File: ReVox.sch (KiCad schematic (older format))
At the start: 43 parts, among them CN1 EXPANSION_PORT, CN2 AUDIO_OUT, CN3 AUDIO_OUT, U1 GAL20V8, U2 74LS273, U3 LM386

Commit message: RIP
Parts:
- removed C6: 100n, Capacitor_THT:C_Disc_D7.0mm_W2.5mm_P5.00mm, symbol Device:C
- added J1: CONN_SIGNALS, ReVox:PinHeader_2x25_P1.27mm_Vertical, symbol Connector_Generic:Conn_02x25_Odd_Even
- CN2, CN3: footprint ReSeed:AudioJack_SJ1-3525N -> ReVox:AudioJack_SJ1-3525N
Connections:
- net +5V: now also J1.3 (Pin_3), J1.5 (Pin_5)
- net GND: now also J1.1 (Pin_1), J1.2 (Pin_2), J1.49 (Pin_49), J1.50 (Pin_50)
- net a0: now also J1.42 (Pin_42)
- net a1: now also J1.40 (Pin_40)
- net a10: now also J1.22 (Pin_22)
- net a11: now also J1.20 (Pin_20)
- net a12: now also J1.18 (Pin_18)
- net a13: now also J1.16 (Pin_16)
- net a14: now also J1.14 (Pin_14)
- net a15: now also J1.12 (Pin_12)
- net a2: now also J1.38 (Pin_38)
- net a3: now also J1.36 (Pin_36)
- net a4: now also J1.34 (Pin_34)
- net a5: now also J1.32 (Pin_32)
- net a6: now also J1.30 (Pin_30)
- net a7: now also J1.28 (Pin_28)
- net a8: now also J1.26 (Pin_26)
- net a9: now also J1.24 (Pin_24)
- net d0: now also J1.41 (Pin_41)
- net d1: now also J1.39 (Pin_39)
- net d2: now also J1.37 (Pin_37)
- net d3: now also J1.35 (Pin_35)
- net d4: now also J1.33 (Pin_33)
- net d5: now also J1.31 (Pin_31)
- net d6: now also J1.29 (Pin_29)
- net d7: now also J1.27 (Pin_27)
- net ext_audio: now also J1.45 (Pin_45)
- net phi2: now also J1.47 (Pin_47)
- net r_~w: now also J1.9 (Pin_9)
- net ~reset: now also J1.6 (Pin_6)
- net ~cs0: now reaches CN1.10 (/CS0)
- net ~cs0: now also J1.19 (Pin_19)
- net ~cas: now reaches CN1.11 (/CAS)
- net ~cas: now also J1.21 (Pin_21)
- net mux: now reaches CN1.12 (MUX)
- net mux: now also J1.23 (Pin_23)
- net ba: now reaches CN1.13 (BA)
- net ba: now also J1.25 (Pin_25)
- net aec: now reaches CN1.22 (AEC)
- net aec: now also J1.43 (Pin_43)
- net ~irq: now reaches CN1.4 (/IRQ)
- net ~irq: now also J1.7 (Pin_7)
- net c1hi: now reaches CN1.6 (C1HI)
- net c1hi: now also J1.11 (Pin_11)
- net c2lo: now reaches CN1.7 (C2LOW)
- net c2lo: now also J1.13 (Pin_13)
- net c2hi: now reaches CN1.8 (C2HI)
- net c2hi: now also J1.15 (Pin_15)
- net ~cs1: now reaches CN1.9 (/CS1)
- net ~cs1: now also J1.17 (Pin_17)
- net aa: now reaches CN1.AA (NC)
- net aa: now also J1.46 (Pin_46)
- net c1lo: now reaches CN1.B (C1LOW)
- net c1lo: now also J1.4 (Pin_4)
- net bb: now reaches CN1.BB (NC)
- net bb: now also J1.48 (Pin_48)
- net ~ras: now reaches CN1.D (/RAS)
- net ~ras: now also J1.8 (Pin_8)
- net phi0: now reaches CN1.E (PHI0)
- net phi0: now also J1.10 (Pin_10)
- net z: now reaches CN1.Z (NC)
- net z: now also J1.44 (Pin_44)
- no-connect marks 17 -> 4
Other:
- note added: "HELPS WITH SCOPING\nAND ROUTING"
- moved on the sheet: CN1, JP1, U1, U2

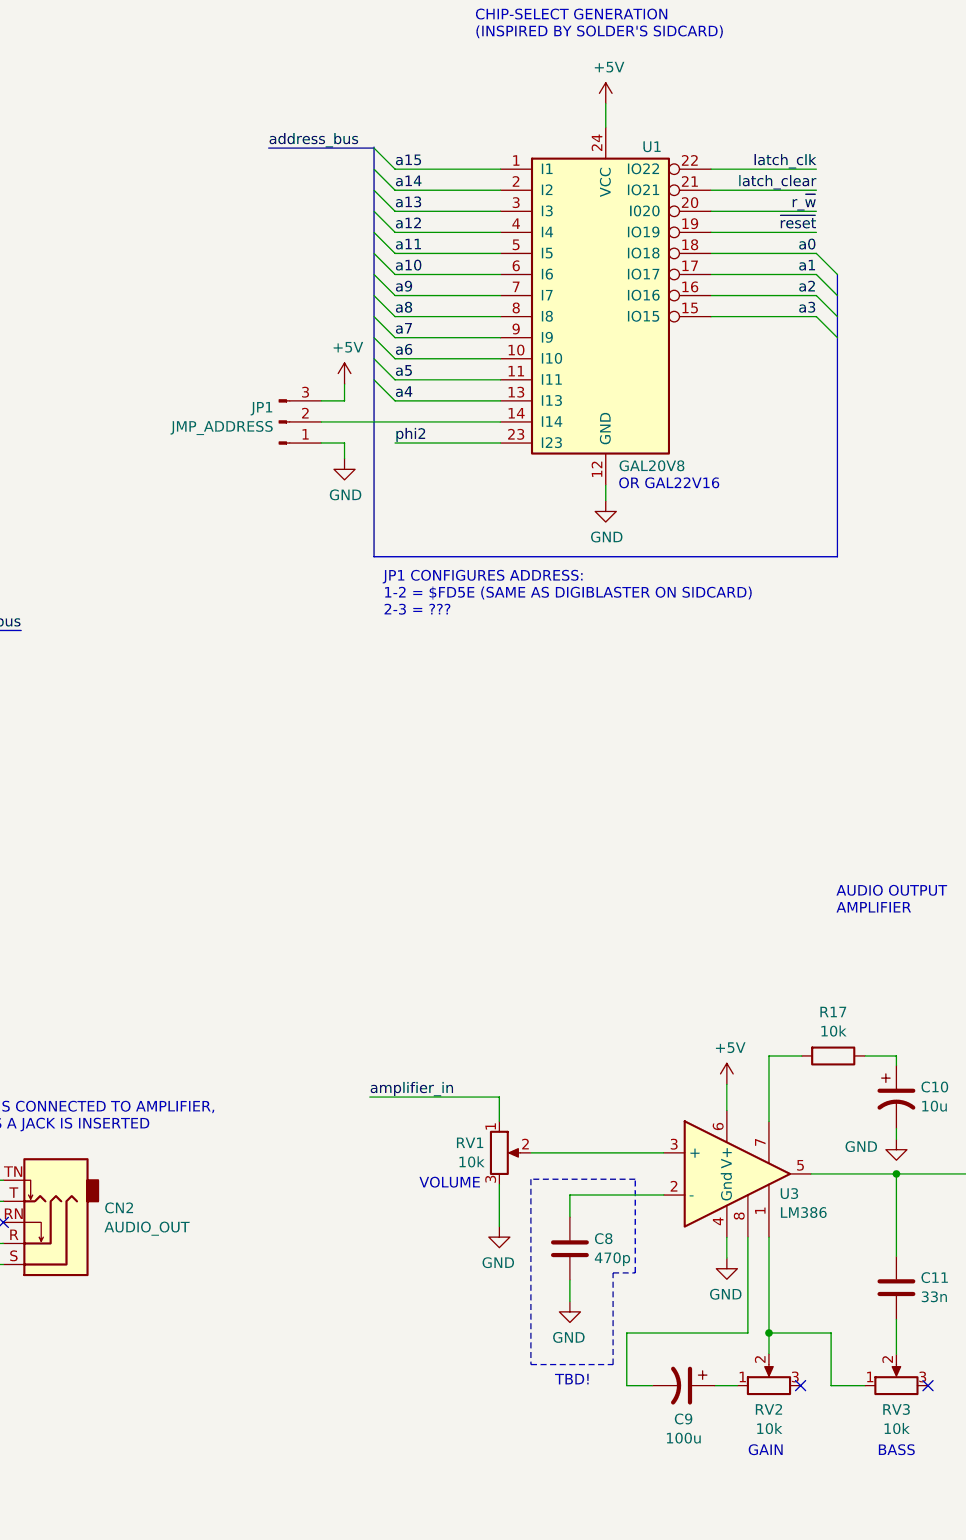
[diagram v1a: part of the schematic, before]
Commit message: First routing pass completed
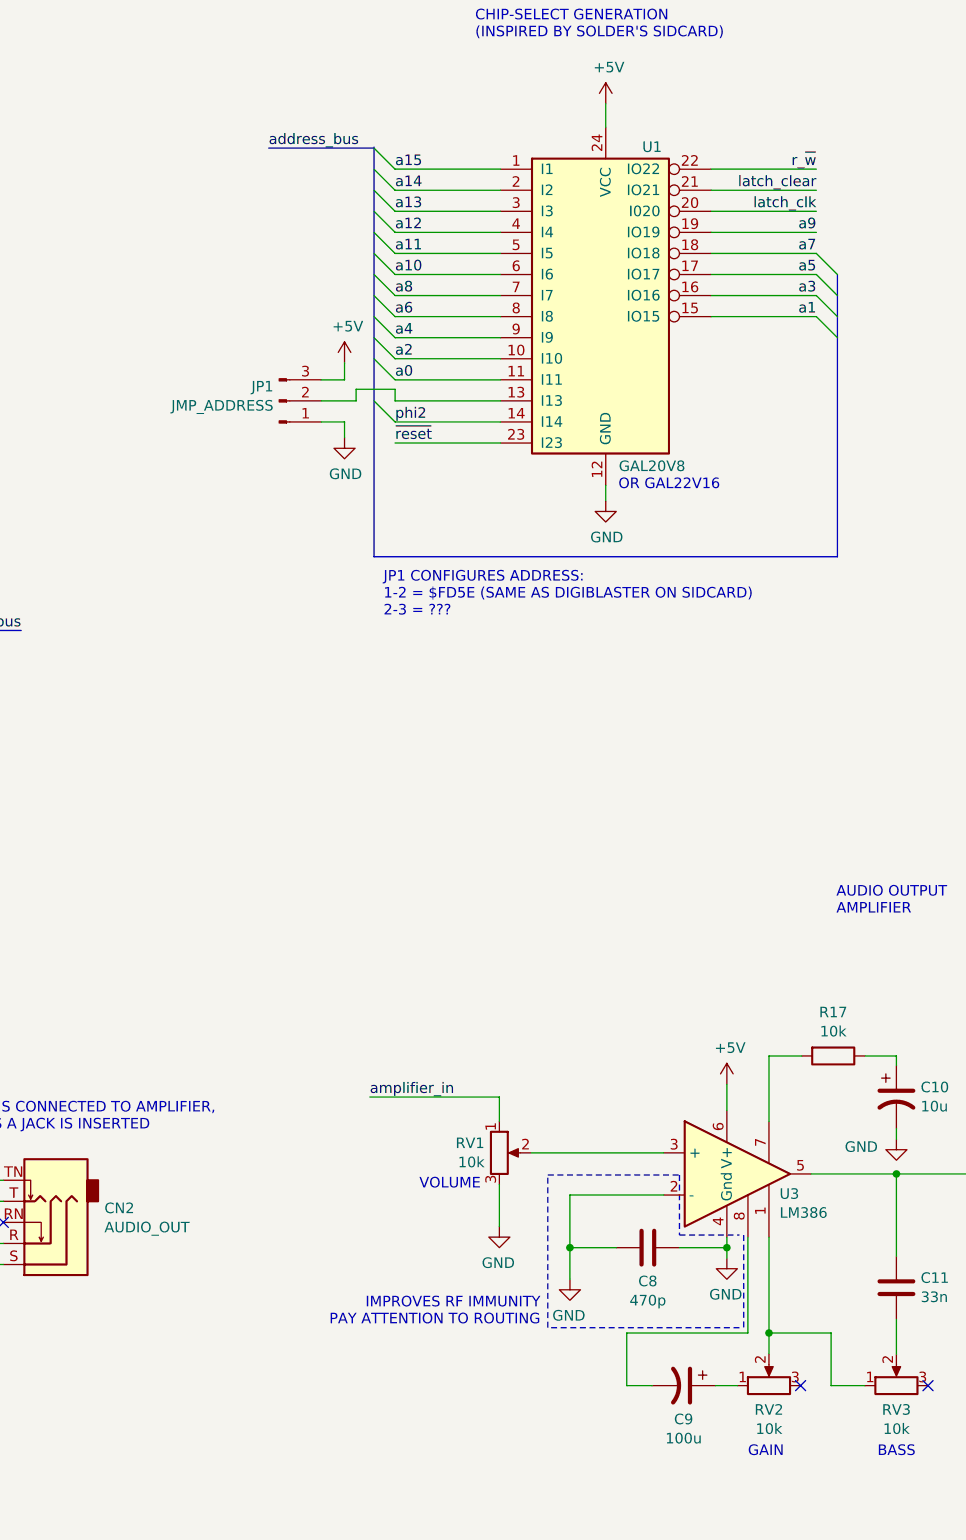
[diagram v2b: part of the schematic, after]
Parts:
- J1: footprint ReVox:PinHeader_2x25_P1.27mm_Vertical -> (none)
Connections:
- net GND: now also C8.2, U3.2 (-)
- net a0: now also U1.11 (I11); no longer U1.18 (IO18)
- net a1: now also U1.15 (IO15); no longer U1.17 (IO17)
- net a2: now also U1.10 (I10); no longer U1.16 (IO16)
- net a3: now also U1.16 (IO16); no longer U1.15 (IO15)
- net a4: now also U1.9 (I9); no longer U1.13 (I13)
- net a5: now also U1.17 (IO17); no longer U1.11 (I11)
- net a6: now also U1.8 (I8); no longer U1.10 (I10)
- net a7: now also U1.18 (IO18); no longer U1.9 (I9)
- net a8: now also U1.7 (I7); no longer U1.8 (I8)
- net a9: now also U1.19 (IO19); no longer U1.7 (I7)
- net latch_clk: now also U1.20 (I020); no longer U1.22 (IO22)
- net phi2: now also U1.14 (I14); no longer U1.23 (I23)
- net r_~w: now also U1.22 (IO22); no longer U1.20 (I020)
- net ~reset: now also U1.23 (I23); no longer U1.19 (IO19)
- net at JP1.2 (Pin_2): now also U1.13 (I13); no longer U1.14 (I14)
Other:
- note added: "IMPROVES RF IMMUNITY\nPAY ATTENTION TO ROUTING"
- note removed: "TBD!"
- moved on the sheet: C8, JP1
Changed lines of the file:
@@
 	9365 1485 9465 1585
 Text Label 9465 2385 0    50   ~ 0
-a7
+a4
 Text Label 9465 2285 0    50   ~ 0
+a6
+Text Label 9465 2185 0    50   ~ 0
 a8
-Text Label 9465 2185 0    50   ~ 0
-a9
 Text Label 9465 2085 0    50   ~ 0
 a10
@@
 	9365 2385 9465 2485
 Text Label 9465 2585 0    50   ~ 0
-a5
+a0
 Text Label 9465 2485 0    50   ~ 0
-a6
-Wire Wire Line
-	9965 2685 9465 2685
-Entry Wire Line
-	9365 2585 9465 2685
-Text Label 9465 2685 0    50   ~ 0
-a4
+a2
+Wire Wire Line
+	9965 2785 9465 2785
+Entry Wire Line
+	9365 2685 9465 2785
 Wire Wire Line
 	9965 2885 9465 2885
-Text Label 9465 2885 0    50   ~ 0
+Text Label 9465 2785 0    50   ~ 0
 phi2
 Wire Wire Line
@@
 Wire Wire Line
 	11465 2185 10965 2185
-Text Label 11465 2185 2    50   ~ 0
-a2
 Text Label 11465 2285 2    50   ~ 0
-a3
+a1
 Wire Wire Line
 	10965 1585 11465 1585
@@
 Text Label 11465 1685 2    50   ~ 0
 latch_clear
-Text Label 11465 1885 2    50   ~ 0
+Text Label 9465 2885 0    50   ~ 0
 ~reset
 $Comp
 L Connector:Conn_01x03_Male JP1
 U 1 1 63A6BB80
-P 8915 2785
-F 0 "JP1" H 8888 2717 50  0000 R CNN
-F 1 "JMP_ADDRESS" H 8888 2808 50  0000 R CNN
-F 2 "Connector_PinHeader_2.54mm:PinHeader_1x03_P2.54mm_Vertical" H 8915 2785 50  0001 C CNN
-F 3 "~" H 8915 2785 50  0001 C CNN
-	1    8915 2785
+P 8915 2685
+F 0 "JP1" H 8888 2617 50  0000 R CNN
+F 1 "JMP_ADDRESS" H 8888 2708 50  0000 R CNN
+F 2 "Connector_PinHeader_2.54mm:PinHeader_1x03_P2.54mm_Vertical" H 8915 2685 50  0001 C CNN
+F 3 "~" H 8915 2685 50  0001 C CNN
+	1    8915 2685
 	1    0    0    1
 $EndComp
 Wire Wire Line
-	9115 2785 9965 2785
-Wire Wire Line
-	9115 2685 9225 2685
-Wire Wire Line
-	9115 2885 9225 2885
-Wire Wire Line
-	9225 2885 9225 2960
+	9115 2585 9225 2585
+Wire Wire Line
+	9115 2785 9225 2785
+Wire Wire Line
+	9225 2785 9225 2860
 $Comp
 L power:GND #PWR015
 U 1 1 63AF3EDD
-P 9225 2960
-F 0 "#PWR015" H 9225 2710 50  0001 C CNN
-F 1 "GND" H 9230 2787 50  0000 C CNN
-F 2 "" H 9225 2960 50  0001 C CNN
-F 3 "" H 9225 2960 50  0001 C CNN
-	1    9225 2960
-	1    0    0    -1
-$EndComp
-Wire Wire Line
-	9225 2605 9225 2685
+P 9225 2860
+F 0 "#PWR015" H 9225 2610 50  0001 C CNN
+F 1 "GND" H 9230 2687 50  0000 C CNN
+F 2 "" H 9225 2860 50  0001 C CNN
+F 3 "" H 9225 2860 50  0001 C CNN
+	1    9225 2860
+	1    0    0    -1
+$EndComp
+Wire Wire Line
+	9225 2505 9225 2585
 $Comp
 L power:+5V #PWR014
 U 1 1 63B0F986
-P 9225 2605
-F 0 "#PWR014" H 9225 2455 50  0001 C CNN
-F 1 "+5V" H 9240 2778 50  0000 C CNN
-F 2 "" H 9225 2605 50  0001 C CNN
-F 3 "" H 9225 2605 50  0001 C CNN
-	1    9225 2605
+P 9225 2505
+F 0 "#PWR014" H 9225 2355 50  0001 C CNN
+F 1 "+5V" H 9240 2678 50  0000 C CNN
+F 2 "" H 9225 2505 50  0001 C CNN
+F 3 "" H 9225 2505 50  0001 C CNN
+	1    9225 2505
 	1    0    0    -1
 $EndComp
@@
 	10965 1985 11465 1985
 Text Label 11465 2085 2    50   ~ 0
-a1
+a5
 Text Label 11465 1985 2    50   ~ 0
-a0
+a7
 $Comp
 L Device:R R1
@@
 $EndComp
 Wire Wire Line
-	11040 6655 11040 6755
+	11040 6655 11040 6705
 $Comp
 L power:GND #PWR022
@@
 $EndComp
 $Comp
-L Device:R_POT RV1
-U 1 1 64B82196
-P 9960 6255
-F 0 "RV1" H 9890 6301 50  0000 R CNN
-F 1 "10k" H 9890 6210 50  0000 R CNN
-F 2 "ReVox:Pot_Bourns_3306P" H 9960 6255 50  0001 C CNN
-F 3 "~" H 9960 6255 50  0001 C CNN
-	1    9960 6255
-	1    0    0    -1
-$EndComp
-$Comp
 L Device:C C4
 U 1 1 64B83085
@@
 L Device:C C8
 U 1 1 64BADB70
-P 10295 6710
-F 0 "C8" H 10180 6664 50  0000 R CNN
-F 1 "470p" H 10180 6755 50  0000 R CNN
-F 2 "Capacitor_THT:C_Disc_D7.0mm_W2.5mm_P5.00mm" H 10333 6560 50  0001 C CNN
-F 3 "~" H 10295 6710 50  0001 C CNN
-	1    10295 6710
-	-1   0    0    1
+P 10665 6705
+F 0 "C8" V 10505 6705 50  0000 C CNN
+F 1 "470p" V 10414 6705 50  0000 C CNN
+F 2 "Capacitor_THT:C_Disc_D7.0mm_W2.5mm_P5.00mm" H 10703 6555 50  0001 C CNN
+F 3 "~" H 10665 6705 50  0001 C CNN
+	1    10665 6705
+	0    -1   -1   0
 $EndComp
 Wire Wire Line
@@
 Wire Wire Line
 	13045 6355 13850 6355
-Wire Wire Line
-	10295 6560 10295 6455
-Wire Wire Line
-	10295 6860 10295 6960
 $Comp
 L power:GND #PWR020
 U 1 1 6524803C
-P 10295 6960
-F 0 "#PWR020" H 10295 6710 50  0001 C CNN
-F 1 "GND" H 10300 6787 50  0000 C CNN
-F 2 "" H 10295 6960 50  0001 C CNN
-F 3 "" H 10295 6960 50  0001 C CNN
-	1    10295 6960
+P 10295 6855
+F 0 "#PWR020" H 10295 6605 50  0001 C CNN
+F 1 "GND" H 10300 6682 50  0000 C CNN
+F 2 "" H 10295 6855 50  0001 C CNN
+F 3 "" H 10295 6855 50  0001 C CNN
+	1    10295 6855
 	-1   0    0    -1
 $EndComp
@@
 	7605 6785 7490 6785
 Connection ~ 7490 6485
-Text Label 11465 1585 2    50   ~ 0
+Text Label 11465 1785 2    50   ~ 0
 latch_clk
 Wire Wire Line
@@
 Text Label 1510 3875 0    50   ~ 0
 ext_audio
-Text Label 11465 1785 2    50   ~ 0
+Text Label 11465 1585 2    50   ~ 0
 r_~w
 Wire Wire Line
@@
 Wire Wire Line
 	12430 6355 12745 6355
-Wire Notes Line
-	10110 6380 10110 7260
-Wire Notes Line
-	10110 7260 10500 7260
-Wire Notes Line
-	10500 7260 10500 6825
-Wire Notes Line
-	10500 6825 10605 6825
-Wire Notes Line
-	10605 6825 10605 6380
-Wire Notes Line
-	10605 6380 10110 6380
-Text Notes 10225 7370 0    50   ~ 0
-TBD!
 $Comp
 L power:+5V #PWR021
@@
 F 0 "J1" H 6470 4292 50  0000 C CNN
 F 1 "CONN_SIGNALS" H 6470 4201 50  0000 C CNN
-F 2 "ReVox:PinHeader_2x25_P1.27mm_Vertical" H 6420 2875 50  0001 C CNN
+F 2 "" H 6420 2875 50  0001 C CNN
 F 3 "~" H 6420 2875 50  0001 C CNN
 	1    6420 2875
@@
 	1    0    0    -1
 $EndComp
+Text Notes 6205 1175 0    50   ~ 0
+HELPS WITH SCOPING\nAND ROUTING
+Wire Wire Line
+	9115 2685 9280 2685
+Wire Wire Line
+	9280 2685 9280 2630
+Wire Wire Line
+	9280 2630 9465 2630
+Wire Wire Line
+	9465 2630 9465 2685
+Wire Wire Line
+	9465 2685 9965 2685
+Text Label 11465 2185 2    50   ~ 0
+a3
+Text Label 11465 1885 2    50   ~ 0
+a9
+$Comp
+L Device:R_POT RV1
+U 1 1 64B82196
+P 9960 6255
+F 0 "RV1" H 9890 6301 50  0000 R CNN
+F 1 "10k" H 9890 6210 50  0000 R CNN
+F 2 "ReVox:Pot_Bourns_3306P" H 9960 6255 50  0001 C CNN
+F 3 "~" H 9960 6255 50  0001 C CNN
+	1    9960 6255
+	1    0    0    -1
+$EndComp
+Wire Wire Line
+	10295 6455 10295 6705
+Wire Wire Line
+	10515 6705 10295 6705
+Connection ~ 10295 6705
+Wire Wire Line
+	10295 6705 10295 6855
+Wire Wire Line
+	10815 6705 11040 6705
+Connection ~ 11040 6705
+Wire Wire Line
+	11040 6705 11040 6755
+Wire Notes Line
+	10190 6360 10815 6360
+Wire Notes Line
+	10815 6360 10815 6645
+Wire Notes Line
+	10815 6645 11100 6645
+Wire Notes Line
+	11120 6645 11120 7085
+Wire Notes Line
+	11100 7085 10190 7085
+Wire Notes Line
+	10190 7085 10190 6360
 Wire Bus Line
 	11565 2085 11565 3425
@@
 Wire Bus Line
 	7165 2275 7165 3775
-Text Notes 6205 1175 0    50   ~ 0
-HELPS WITH SCOPING\nAND ROUTING
+Text Notes 10155 7080 2    50   ~ 0
+IMPROVES RF IMMUNITY\nPAY ATTENTION TO ROUTING
 $EndSCHEMATC
